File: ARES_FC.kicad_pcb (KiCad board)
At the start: 2 copper layers, 57.2 x 57.2 mm, 67 parts, among them J1 SWD, J2 TYPE-C-31-M-12, J3 FC_M/P, J4 5V, J5 GND, J6 FC_RF, J7 Conn_01x04_Pin, J8 Conn_01x04_Pin, U1 STM32F401CCU6, U2 AMS1117-3.3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

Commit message: added gps antenna shielding
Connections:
- AE1 pad 2: (no net) -> GND

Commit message: added gerbers & CPL for ordering
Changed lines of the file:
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@@
 			(plot_on_all_layers_selection 0x0000000_00000000)
 			(disableapertmacros no)
-			(usegerberextensions no)
-			(usegerberattributes yes)
-			(usegerberadvancedattributes yes)
-			(creategerberjobfile yes)
+			(usegerberextensions yes)
+			(usegerberattributes no)
+			(usegerberadvancedattributes no)
+			(creategerberjobfile no)
 			(dashed_line_dash_ratio 12.000000)
 			(dashed_line_gap_ratio 3.000000)
@@
 			(psa4output no)
 			(plotreference yes)
-			(plotvalue yes)
+			(plotvalue no)
 			(plotfptext yes)
 			(plotinvisibletext no)
 			(sketchpadsonfab no)
-			(subtractmaskfromsilk no)
+			(subtractmaskfromsilk yes)
 			(outputformat 1)
 			(mirror no)
@@
 				(font
 					(size 1.27 1.27)
+					(thickness 0.15)
 				)
 			)
@@
 				(font
 					(size 1.27 1.27)
+					(thickness 0.15)
 				)
 			)
@@
 				(font
 					(size 1.27 1.27)
+					(thickness 0.15)
 				)
 			)
@@
 	)
 	(segment
-		(start 142.487653 92.737653)
-		(end 142.675 92.550305)
+		(start 147.1625 91.79974)
+		(end 143.12029 91.79974)
 		(width 0.25)
 		(layer "F.Cu")
@@
 	)
 	(segment
-		(start 141.716766 93.50854)
-		(end 142.487653 92.737653)
+		(start 142.675 92.550305)
+		(end 141.716765 93.50854)
 		(width 0.25)
 		(layer "F.Cu")
@@
 	)
 	(segment
-		(start 143.12029 91.79974)
-		(end 147.1625 91.79974)
+		(start 141.716765 93.50854)
+		(end 141 93.50854)
 		(width 0.25)
 		(layer "F.Cu")
@@
 	(segment
 		(start 142.675 92.24503)
-		(end 143.12029 91.79974)
-		(width 0.25)
-		(layer "F.Cu")
-		(net 4)
-	)
-	(segment
-		(start 141 93.50854)
-		(end 141.716766 93.50854)
+		(end 142.675 92.550305)
 		(width 0.25)
 		(layer "F.Cu")
@@
 	)
 	(segment
-		(start 142.675 92.550305)
+		(start 143.12029 91.79974)
 		(end 142.675 92.24503)
 		(width 0.25)
@@
 	)
 	(segment
-		(start 142.250305 92.975)
-		(end 142.487653 92.737653)
-		(width 0.25)
-		(layer "F.Cu")
-		(net 4)
-	)
-	(segment
 		(start 142.65 79.2)
 		(end 145.375 76.475)
@@
 	)
 	(segment
+		(start 156.80026 91.29974)
+		(end 154.0375 91.29974)
+		(width 0.2)
+		(layer "F.Cu")
+		(net 13)
+	)
+	(segment
 		(start 171.2625 99.53)
 		(end 171.2625 100.07)
@@
 	)
 	(segment
-		(start 154.6 91.29974)
-		(end 154.693751 91.29974)
-		(width 0.2)
-		(layer "F.Cu")
-		(net 13)
-	)
-	(segment
-		(start 154.0375 91.29974)
-		(end 154.6 91.29974)
-		(width 0.2)
-		(layer "F.Cu")
-		(net 13)
-	)
-	(segment
-		(start 156.80026 91.29974)
-		(end 154.6 91.29974)
-		(width 0.2)
-		(layer "F.Cu")
-		(net 13)
-	)
-	(segment
 		(start 171.2625 100.07)
 		(end 171.4925 100.3)
@@
 	)
 	(segment
-		(start 157.15 90.95)
-		(end 156.80026 91.29974)
-		(width 0.2)
-		(layer "F.Cu")
-		(net 13)
-	)
-	(segment
 		(start 170.15 99.3)
 		(end 172.3125 99.3)
@@
 		(width 0.2)
 		(layer "F.Cu")
+		(net 13)
+	)
+	(segment
+		(start 157.15 90.95)
+		(end 156.80026 91.29974)
+		(width 0.2)
+		(layer "F.Cu")

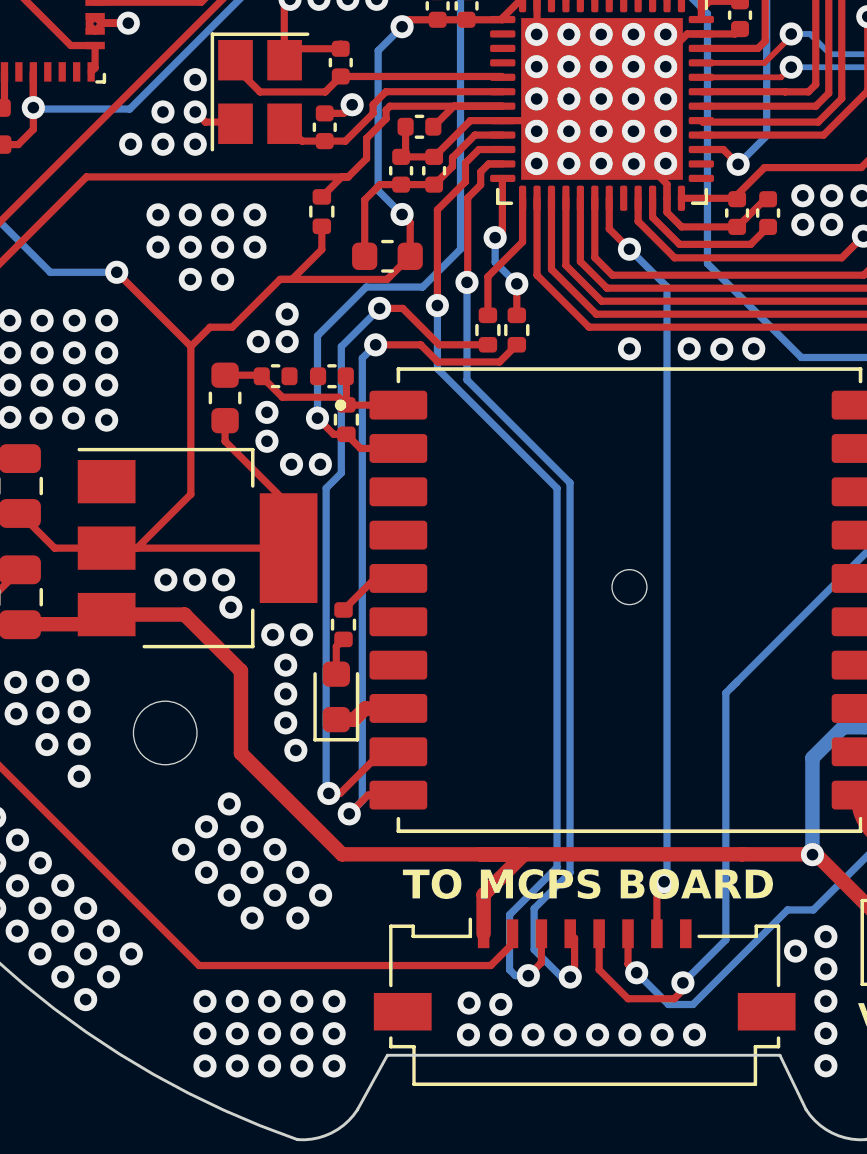
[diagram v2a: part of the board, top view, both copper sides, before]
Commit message: removed pullup resistor on NRST
There is already an internal pullup according to the datasheet
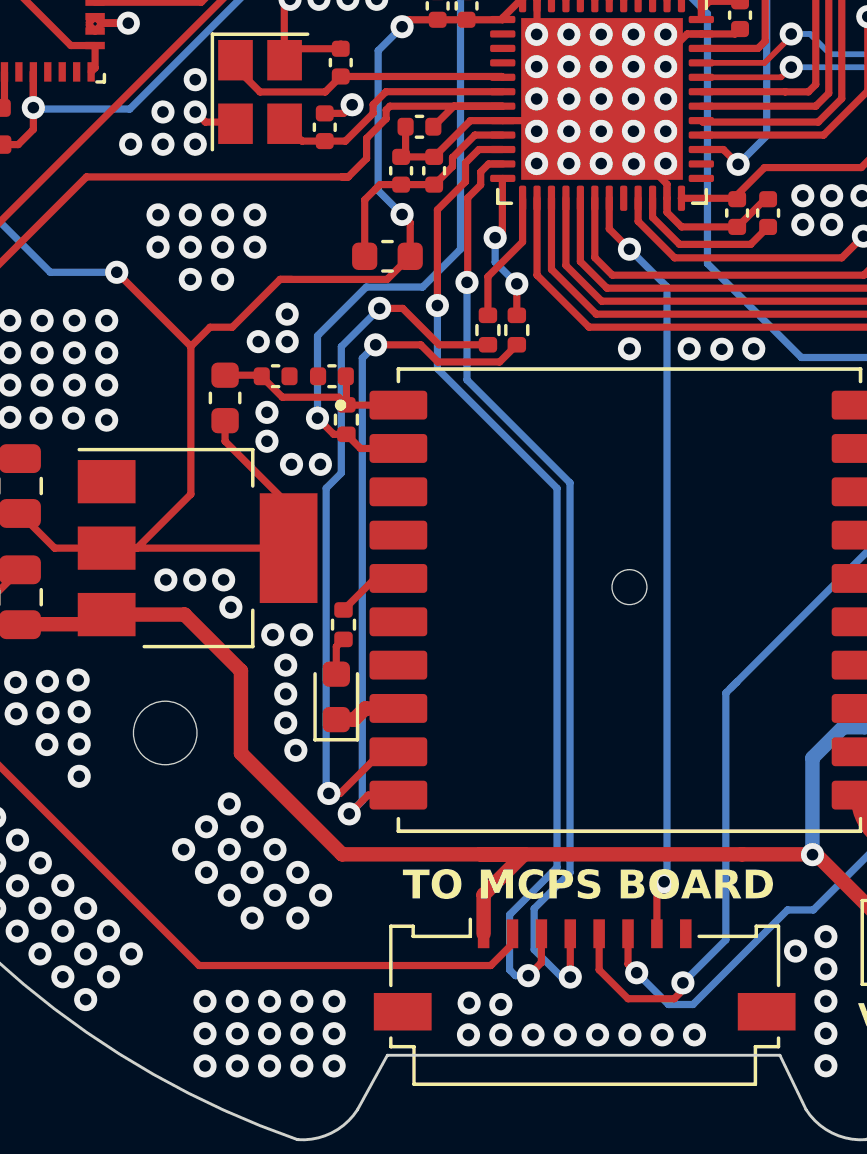
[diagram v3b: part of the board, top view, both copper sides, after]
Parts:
- removed R14: 10k, Resistor_SMD:R_0402_1005Metric
- renumbered C14 to C13, C13 to C14
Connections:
- C1 pad 1: /NRST -> GND
- C1 pad 2: GND -> /NRST
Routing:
- net +3.3V: track 234.9 -> 232.6 mm
- net /NRST: track 32.7 -> 31.8 mm

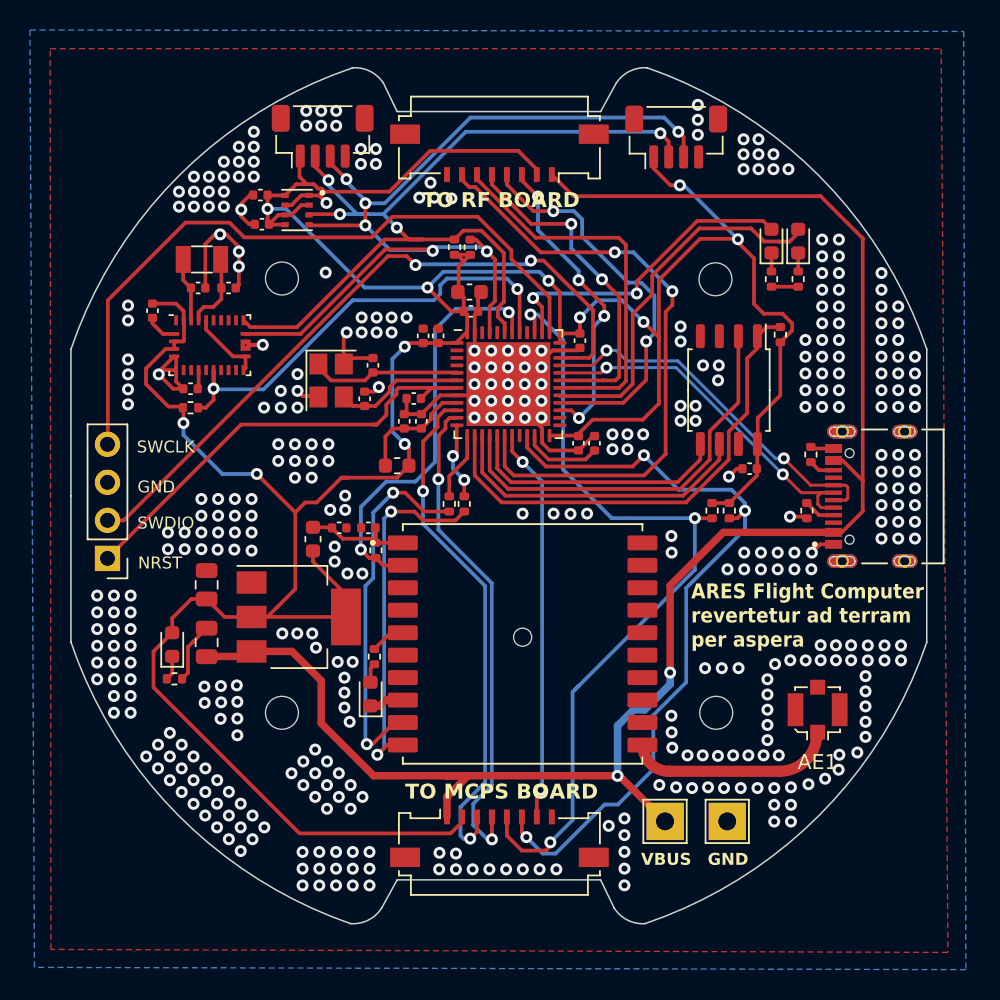
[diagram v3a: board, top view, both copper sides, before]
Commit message: changed grown plane to solid and cleaned traces
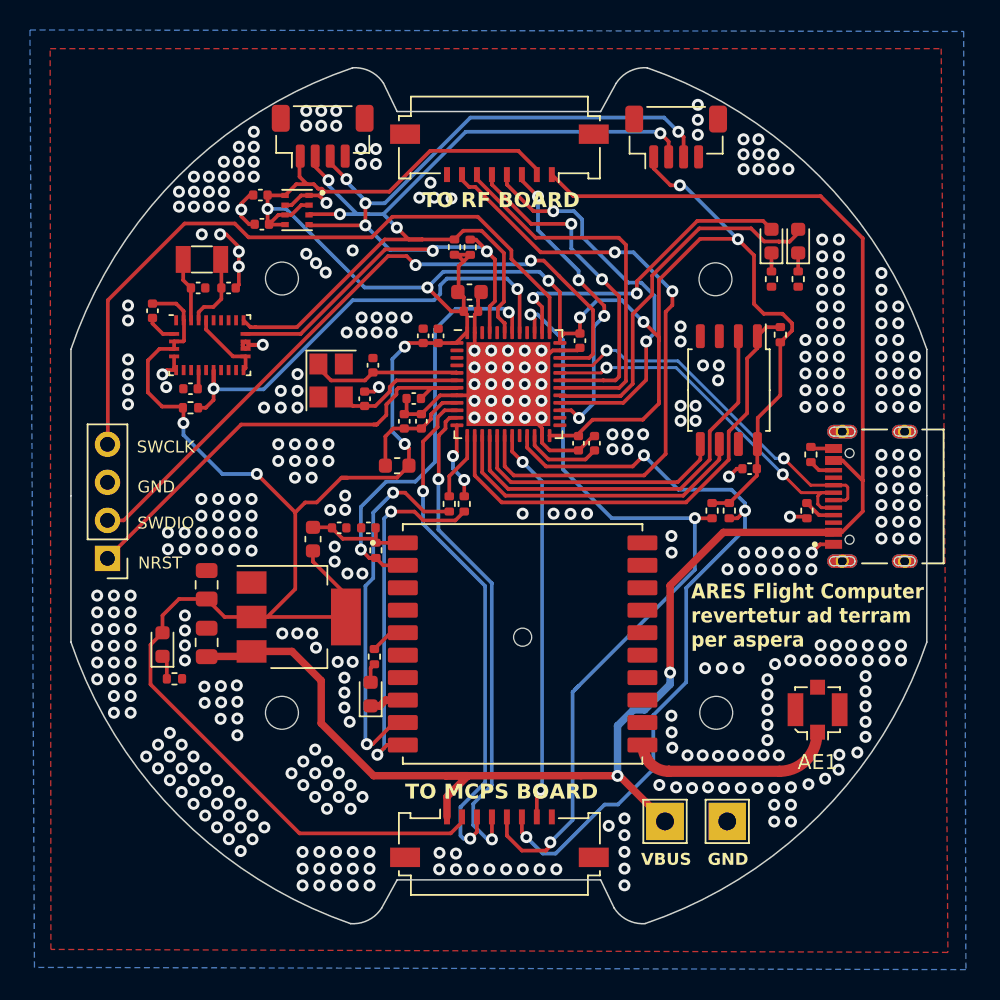
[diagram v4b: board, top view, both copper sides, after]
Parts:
- moved D1 0.65 mm to (127.5, 109.4)
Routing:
- net GND: track 81.0 -> 60.7 mm, vias 403 -> 412
- net +3.3V: track 232.6 -> 233.7 mm

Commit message: cleaned layout (ground layer -> solid)
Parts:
- turned C1 to 0 degrees
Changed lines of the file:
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@@
 	(footprint "Capacitor_SMD:C_0402_1005Metric"
 		(layer "F.Cu")
-		(at 144.28 93.011 180)
+		(at 144.28 93.011)
 		(descr "Capacitor SMD 0402 (1005 Metric), square (rectangular) end terminal, IPC_7351 nominal, (Body size source: IPC-SM-782 page 76, https://www.pcb-3d.com/wordpress/wp-content/uploads/ipc-sm-782a_amendment_1_and_2.pdf), generated with kicad-footprint-generator")
 		(tags "capacitor")
 		(property "Reference" "C1"
-			(at -0.12 1.111 0)
+			(at -0.12 1.111 360)
 			(layer "F.SilkS")
 			(hide yes)
@@
 		)
 		(property "Value" "100nF"
-			(at 0 1.16 0)
+			(at 0 1.16 360)
 			(layer "F.Fab")
 			(effects
@@
 		)
 		(property "Footprint" "Capacitor_SMD:C_0402_1005Metric"
-			(at 0 0 180)
+			(at 0 0 0)
 			(unlocked yes)
 			(layer "F.Fab")
@@
 		)
 		(property "Datasheet" ""
-			(at 0 0 180)
+			(at 0 0 0)
 			(unlocked yes)
 			(layer "F.Fab")
@@
 		)
 		(property "Description" ""
-			(at 0 0 180)
+			(at 0 0 0)
 			(unlocked yes)
 			(layer "F.Fab")
@@
 		)
 		(property "LCSC Part" "C307331"
-			(at 0 0 180)
+			(at 0 0 0)
 			(unlocked yes)
 			(layer "F.Fab")
@@
 		(attr smd)
 		(fp_line
+			(start -0.107836 -0.36)
+			(end 0.107836 -0.36)
+			(stroke
+				(width 0.12)
+				(type solid)
+			)
+			(layer "F.SilkS")
+		)
+		(fp_line
 			(start -0.107836 0.36)
 			(end 0.107836 0.36)
@@
 		)
 		(fp_line
-			(start -0.107836 -0.36)
-			(end 0.107836 -0.36)
+			(start -0.91 -0.46)
+			(end 0.91 -0.46)
 			(stroke
-				(width 0.12)
+				(width 0.05)
 				(type solid)
 			)
-			(layer "F.SilkS")
+			(layer "F.CrtYd")
 		)
 		(fp_line
-			(start 0.91 0.46)
-			(end -0.91 0.46)
+			(start -0.91 0.46)
+			(end -0.91 -0.46)
 			(stroke
 				(width 0.05)
@@
 		)
 		(fp_line
-			(start -0.91 0.46)
-			(end -0.91 -0.46)
+			(start 0.91 0.46)
+			(end -0.91 0.46)
 			(stroke
 				(width 0.05)
@@
 		)
 		(fp_line
-			(start -0.91 -0.46)
-			(end 0.91 -0.46)
+			(start -0.5 -0.25)
+			(end 0.5 -0.25)
 			(stroke
-				(width 0.05)
+				(width 0.1)
 				(type solid)
 			)
-			(layer "F.CrtYd")
+			(layer "F.Fab")
 		)
 		(fp_line
-			(start 0.5 0.25)
-			(end -0.5 0.25)
+			(start -0.5 0.25)
+			(end -0.5 -0.25)
 			(stroke
 				(width 0.1)
@@
 		)
 		(fp_line
-			(start -0.5 0.25)
-			(end -0.5 -0.25)
-			(stroke
-				(width 0.1)
-				(type solid)
-			)
-			(layer "F.Fab")
-		)
-		(fp_line
-			(start -0.5 -0.25)
-			(end 0.5 -0.25)
+			(start 0.5 0.25)
+			(end -0.5 0.25)
 			(stroke
 				(width 0.1)
@@
 		)
 		(fp_text user "${REFERENCE}"
-			(at 0 0 0)
+			(at 0 0 360)
 			(layer "F.Fab")
 			(effects
@@
 		)
 		(pad "1" smd roundrect
-			(at -0.48 0 180)
+			(at -0.48 0)
 			(size 0.56 0.62)
 			(layers "F.Cu" "F.Paste" "F.Mask")
@@
 		)
 		(pad "2" smd roundrect
-			(at 0.48 0 180)
+			(at 0.48 0)
 			(size 0.56 0.62)
 			(layers "F.Cu" "F.Paste" "F.Mask")

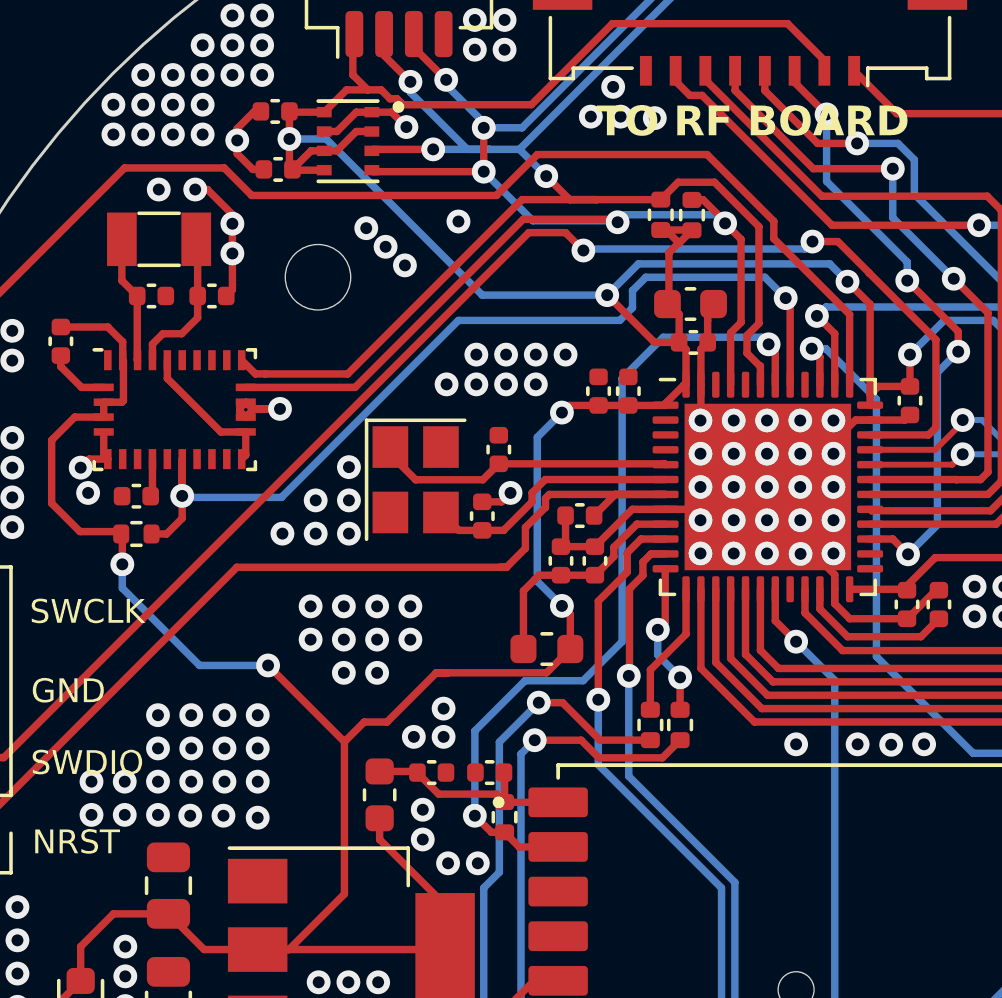
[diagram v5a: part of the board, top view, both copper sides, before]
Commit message: added tvs and boot0
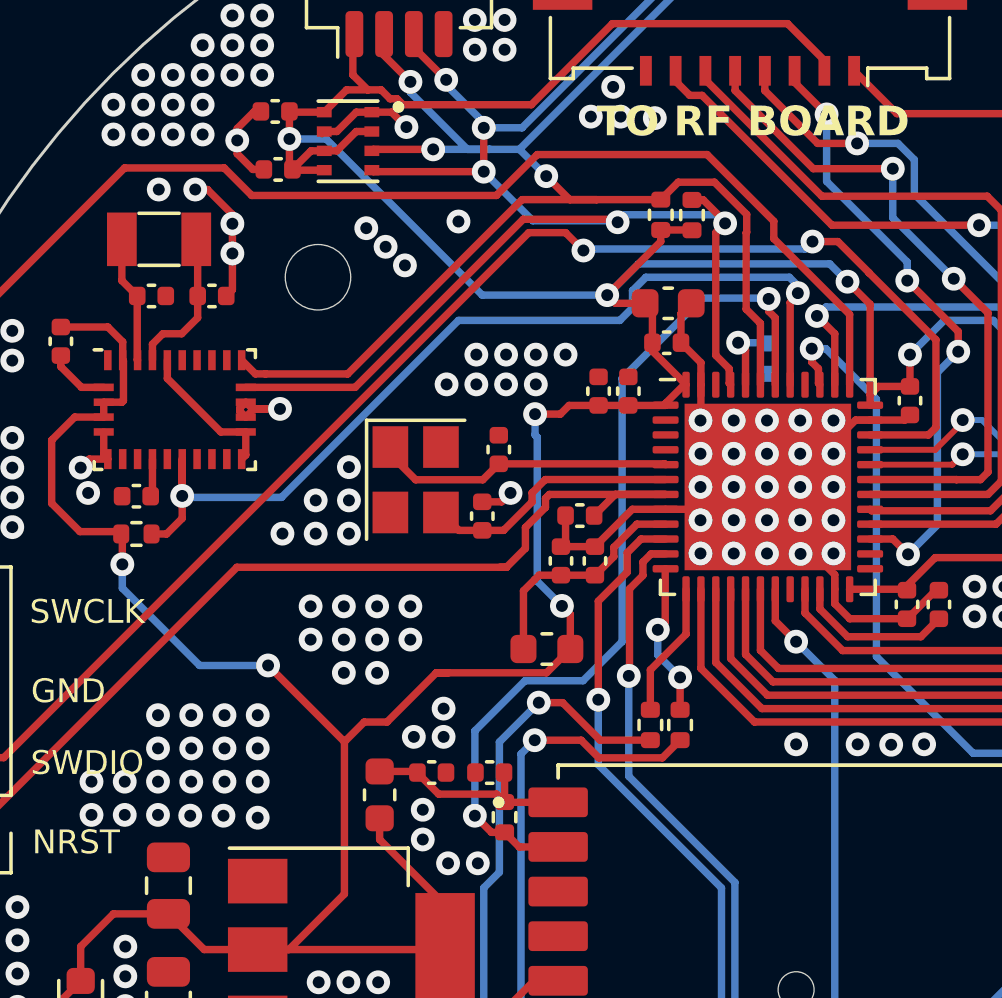
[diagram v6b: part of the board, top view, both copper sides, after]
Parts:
- added R14: 10k, Resistor_SMD:R_0402_1005Metric, B.Cu at (150.7, 87.7)
- moved C8 0.90 mm to (147.2, 87.2)
- moved C4 0.75 mm to (147.2, 85.9)
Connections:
- U1 pad 44: unconnected-(U1-BOOT0-Pad44) -> Net-(U1-BOOT0)
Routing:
- net Net-(U1-BOOT0): track 0.00 -> 2.58 mm, vias 0 -> 1
- net /GPS_NRST: track 28.2 -> 30.2 mm
- net +3.3V: track 233.7 -> 232.2 mm
- net /BNO_NRST: track 31.5 -> 32.2 mm
